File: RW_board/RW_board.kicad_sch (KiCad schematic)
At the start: 2 parts, among them J3 1-84953-1, J4 Conn_01x08_Pin

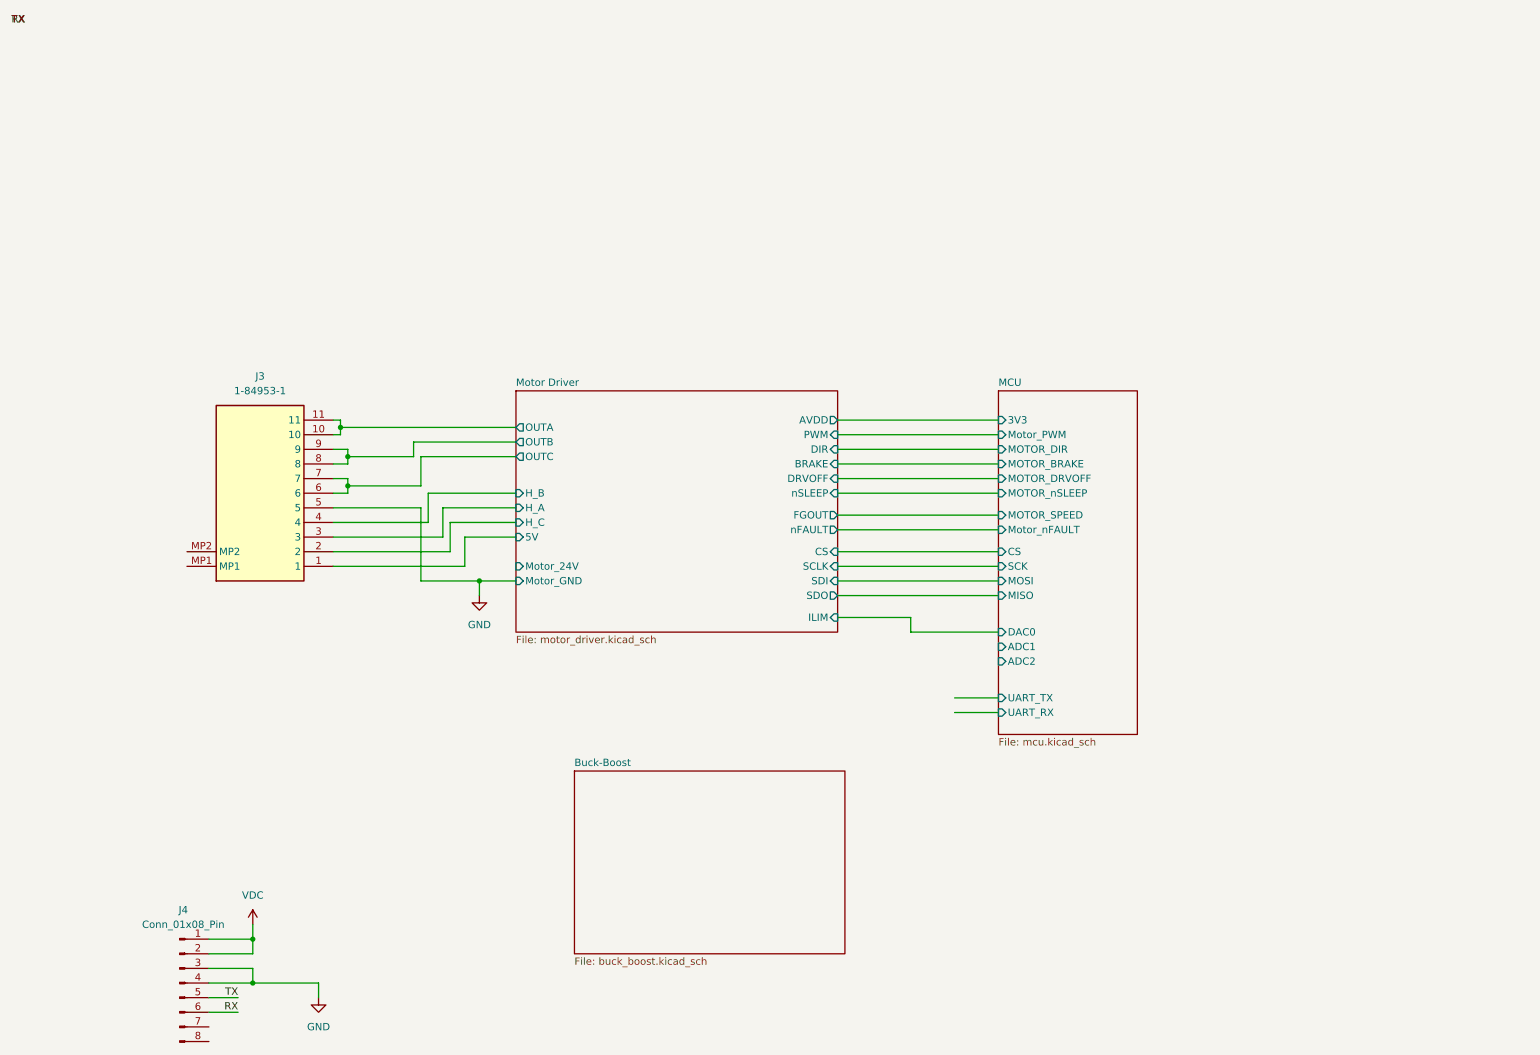
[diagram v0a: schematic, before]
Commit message: Connected everything, added testpoints
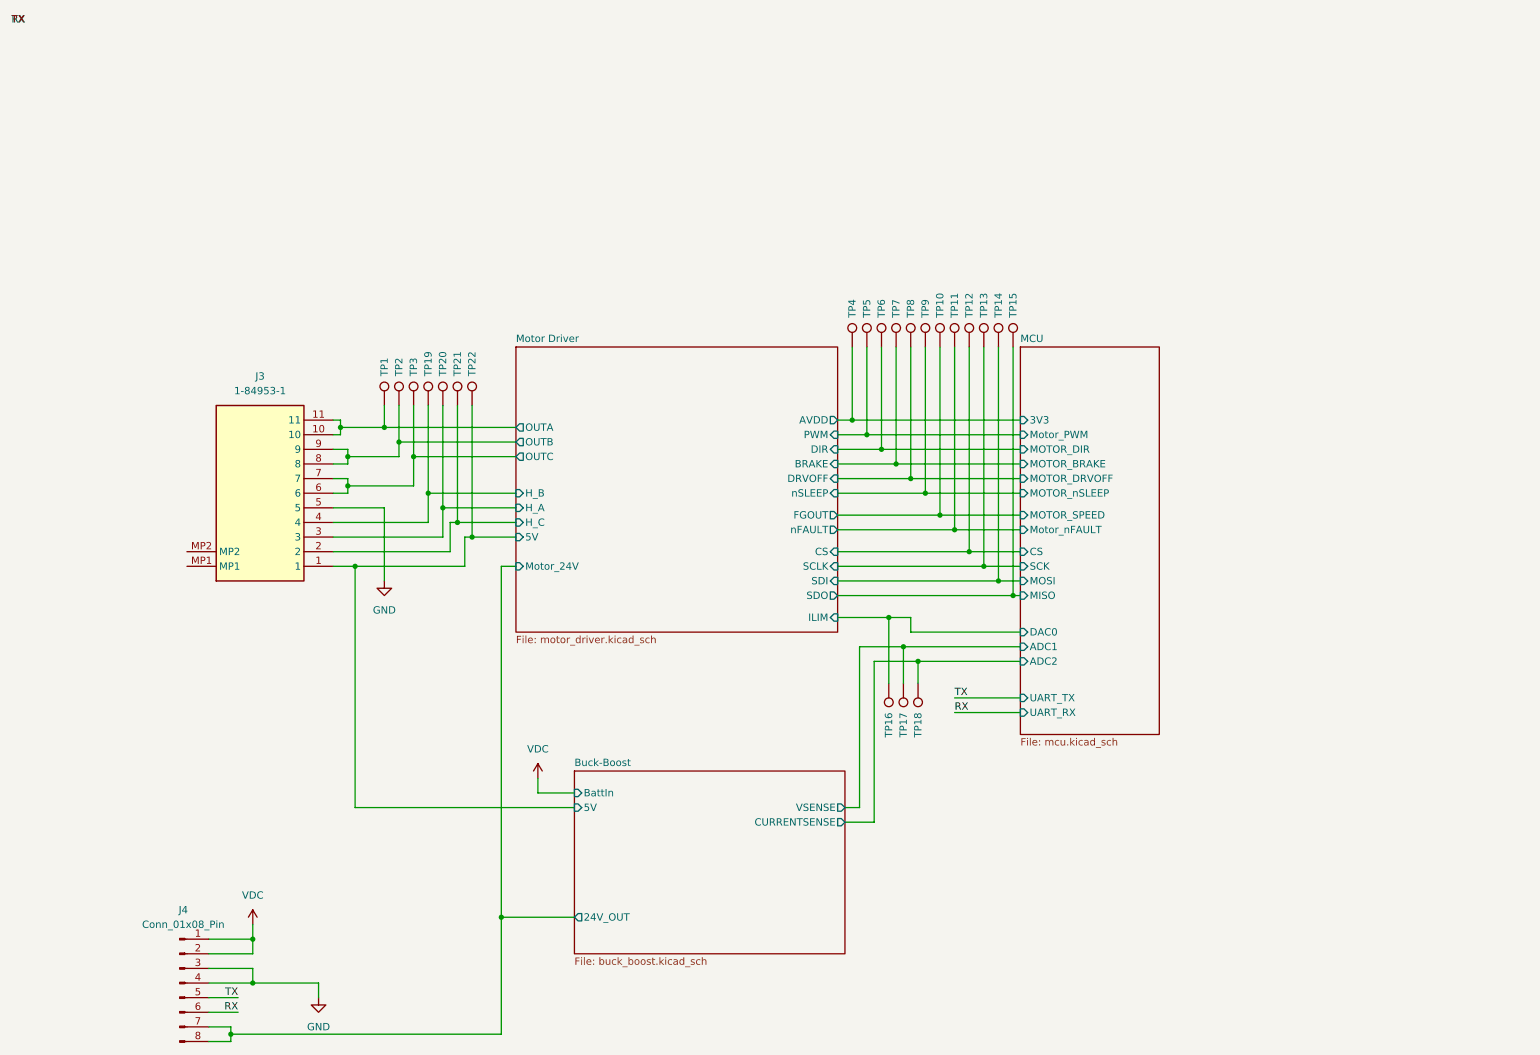
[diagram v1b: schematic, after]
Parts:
- added TP1, TP10, TP11, TP12, TP13, TP14, TP15, TP16, TP17, TP18, TP19, TP2, TP20, TP21, TP22, TP3, TP4, TP5, TP6, TP7, TP8, TP9: TestPoint, TestPoint:TestPoint_Pad_1.0x1.0mm, symbol Connector:TestPoint
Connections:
- net MCU/3V3: now also TP4.1
- net MCU/CS: now also TP12.1
- net MCU/DAC0: now also TP16.1
- net MCU/MISO: now also TP15.1
- net MCU/MOSI: now also TP14.1
- net MCU/MOTOR_BRAKE: now also TP7.1
- net MCU/MOTOR_DIR: now also TP6.1
- net MCU/MOTOR_DRVOFF: now also TP8.1
- net MCU/MOTOR_SPEED: now also TP10.1
- net MCU/MOTOR_nSLEEP: now also TP9.1
- net MCU/Motor_PWM: now also TP5.1
- net MCU/Motor_nFAULT: now also TP11.1
- net MCU/SCK: now also TP13.1
- net Motor Driver/H_A: now also TP20.1
- net Motor Driver/H_B: now also TP19.1
- net Motor Driver/H_C: now also TP21.1
- net Motor Driver/OUTA: now also TP1.1
- net Motor Driver/OUTB: now also TP2.1
- net Motor Driver/OUTC: now also TP3.1
- net Buck-Boost/24V_OUT: now reaches J4.7 (Pin_7)
- net Buck-Boost/24V_OUT: now also J4.8 (Pin_8)
- net Motor Driver/5V renamed Buck-Boost/5V
- net Buck-Boost/5V: now also TP22.1
- new net Buck-Boost/CURRENTSENSE: TP18.1
- new net Buck-Boost/VSENSE: TP17.1
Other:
- sheet Buck-Boost ports: added 24V_OUT, 5V, BattIn, CURRENTSENSE, VSENSE; removed none
- sheet Motor Driver ports: added none; removed Motor_GND

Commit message: Initial board layout
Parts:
- added R101: 10k, Resistor_SMD:R_0402_1005Metric, symbol Device:R
- added R102: 1k, Resistor_SMD:R_0402_1005Metric, symbol Device:R
- renumbered J4 to J1, J3 to J2, TP6 to TP10, TP16 to TP11, TP7 to TP12, TP17 to TP13, TP8 to TP14, TP18 to TP15, TP9 to TP16, TP10 to TP17, TP11 to TP18, TP12 to TP19, TP13 to TP20, TP14 to TP21, TP15 to TP22, TP19 to TP4, TP20 to TP5, TP21 to TP6, TP22 to TP7, TP4 to TP8, TP5 to TP9
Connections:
- net GND: now also R102.2
- net VDC: now also R101.1
- new net MCU/ADC3: R101.2, R102.1
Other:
- sheet MCU ports: added ADC3; removed none

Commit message: Initial routing complete
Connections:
- net RX: no longer J1.6 (Pin_6)
- new net TX: J1.6 (Pin_6)
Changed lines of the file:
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@@
 	)
 	(label "RX"
-		(at 39.37 171.45 180)
-		(fields_autoplaced yes)
-		(effects
-			(font
-				(size 1.27 1.27)
-			)
-			(justify right bottom)
-		)
-	)
-	(label "TX"
-		(at 39.37 168.91 180)
-		(fields_autoplaced yes)
-		(effects
-			(font
-				(size 1.27 1.27)
-			)
-			(justify right bottom)
-		)
-	)
-	(label "TX"
-		(at 0 0 0)
-		(fields_autoplaced yes)
+		(at 163.83 119.38 0)
 		(effects
 			(font
@@
 	(label "TX"
 		(at 163.83 116.84 0)
-		(fields_autoplaced yes)
 		(effects
 			(font
@@
 		)
 	)
-	(label "RX"
-		(at 163.83 119.38 0)
-		(fields_autoplaced yes)
+	(label "TX"
+		(at 39.37 171.45 180)
 		(effects
 			(font
 				(size 1.27 1.27)
 			)
-			(justify left bottom)
+			(justify right bottom)
 		)
 	)
 	(label "RX"
-		(at 0 0 0)
-		(fields_autoplaced yes)
+		(at 39.37 168.91 180)
 		(effects
 			(font
 				(size 1.27 1.27)
 			)
-			(justify left bottom)
+			(justify right bottom)
 		)
 	)

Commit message: Board complete
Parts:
- removed TP10: TestPoint, TestPoint:TestPoint_Pad_1.0x1.0mm, symbol Connector:TestPoint
- added H101, H102, H103, H104: MountingHole_Pad, RW_Imports:MountingHole_3.4mm_Pad, symbol Mechanical:MountingHole_Pad
- added R103, R104, R105, R106: DNP, Resistor_SMD:R_0402_1005Metric, symbol Device:R
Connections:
- net GND: now also R103.2, R104.2, R105.2, R106.2
- new net: H102.1, R104.1
- new net: H103.1, R105.1
- new net: H101.1, R103.1
- new net: H104.1, R106.1
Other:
- moved on the sheet: TP12, TP14, TP16, TP17, TP18, TP19, TP20, TP21, TP22

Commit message: Bom completed and generated, minor PCB adjustments
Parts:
- J1: Mouser Part Number (none) -> 538-53048-0810
- R101: Mouser Part Number (none) -> 710-560112110020
- R102: Mouser Part Number (none) -> 710-560112110012
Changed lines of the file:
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@@
+			)
+		)
+		(property "Mouser Part Number" "710-560112110012 "
+			(at 170.18 148.59 0)
+			(effects
+				(font
+					(size 1.27 1.27)
+				)
+				(hide yes)
 			)
 		)
@@
 			)
 		)
+		(property "Mouser Part Number" "538-53048-0810 "
+			(at 29.21 166.37 0)
+			(effects
+				(font
+					(size 1.27 1.27)
+				)
+				(hide yes)
+			)
+		)
 		(pin "4"
 		)
@@
 			(at 170.18 138.43 0)
 			(effects
+				(font
+					(size 1.27 1.27)
+				)
+				(hide yes)
+			)
+		)
+		(property "Mouser Part Number" "710-560112110020 "
+			(at 170.18 138.43 0)
+			(effects
